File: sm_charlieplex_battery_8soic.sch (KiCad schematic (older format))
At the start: 14 parts, among them SW1 SW_Push, U1 ATtiny10-TS

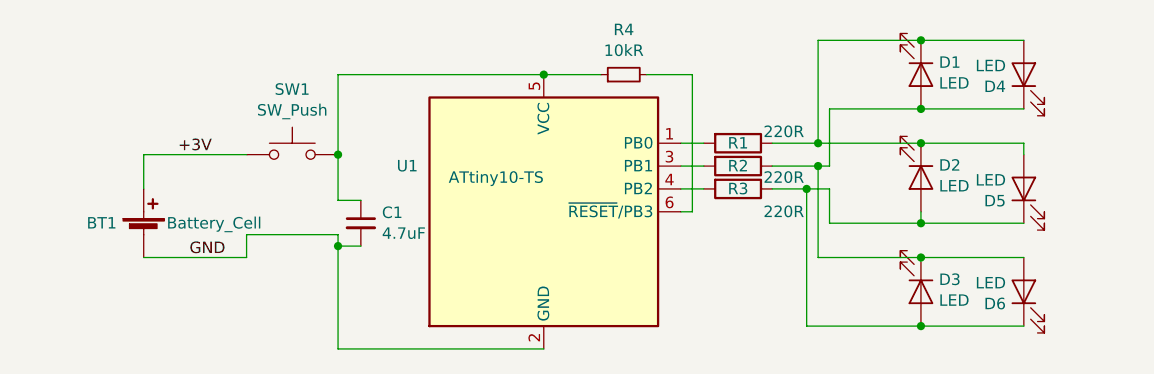
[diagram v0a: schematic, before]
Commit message: Reformat to use ATTiny402
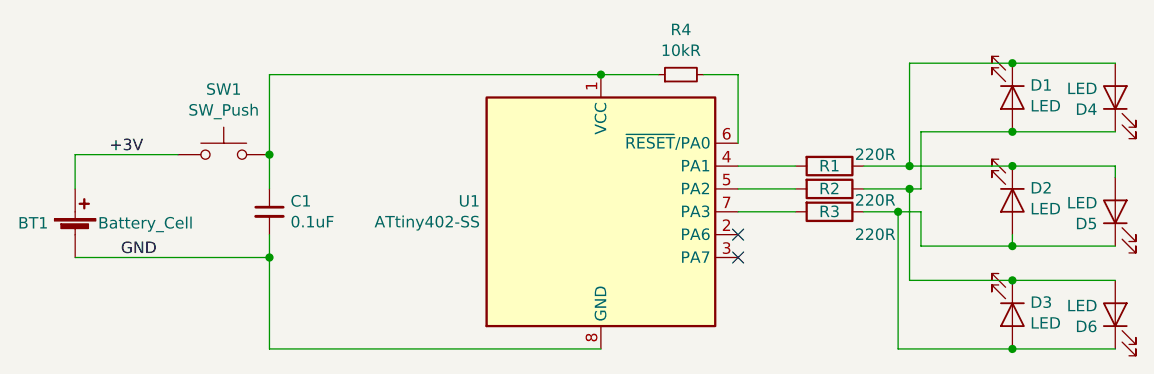
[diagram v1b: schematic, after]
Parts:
- removed U1: ATtiny10-TS, Package_TO_SOT_SMD:SOT-23-6, symbol MCU_Microchip_ATtiny:ATtiny10-TS
- added U1: ATtiny402-SS, Package_SO:SOIC-8_3.9x4.9mm_P1.27mm, symbol MCU_Microchip_ATtiny:ATtiny402-SS
- C1: value 4.7uF -> 0.1uF
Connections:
- net GND: now also U1.8 (GND)
- net at R1.2: now also U1.4 (PA1)
- net at R2.2: now also U1.5 (PA2)
- net at R3.2: now also U1.7 (PA3)
- net at C1.1, R4.1, SW1.2: now also U1.1 (VCC)
- net at R4.2: now also U1.6 (~RESET~/PA0)
- no-connect marks 0 -> 2
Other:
- moved on the sheet: BT1, C1, D1, D2, D3, D4, D5, D6, R1, R2, R3, R4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

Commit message: Some changes
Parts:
- removed U1: ATtiny402-SS, Package_SO:SOIC-8_3.9x4.9mm_P1.27mm, symbol MCU_Microchip_ATtiny:ATtiny402-SS
- added U1: ATtiny13A-SSU, Package_SO:SOIC-8_3.9x4.9mm_P1.27mm, symbol MCU_Microchip_ATtiny:ATtiny13A-SSU
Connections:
- net GND: now also U1.4 (GND)
- net at R1.2: now also U1.6 (PB1)
- net at R2.2: now also U1.7 (PB2)
- net at R3.2: now also U1.2 (PB3)
- net at C1.1, R4.1, SW1.2: now also U1.8 (VCC)
- net at R4.2: now also U1.1 (~RESET~/PB5)
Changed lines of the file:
@@
 Wire Wire Line
 	2850 3500 3300 3500
-$Comp
-L MCU_Microchip_ATtiny:ATtiny402-SS U1
-U 1 1 5DEC46B9
-P 5150 3750
-F 0 "U1" H 4621 3796 50  0000 R CNN
-F 1 "ATtiny402-SS" H 4621 3705 50  0000 R CNN
-F 2 "Package_SO:SOIC-8_3.9x4.9mm_P1.27mm" H 5150 3750 50  0001 C CIN
-F 3 "http://ww1.microchip.com/downloads/en/DeviceDoc/ATtiny202-402-AVR-MCU-with-Core-Independent-Peripherals_and-picoPower-40001969A.pdf" H 5150 3750 50  0001 C CNN
-	1    5150 3750
-	1    0    0    -1
-$EndComp
 Wire Wire Line
 	3700 3950 3700 3850
@@
 Connection ~ 3700 3950
 Wire Wire Line
-	5150 3150 5400 3150
-Connection ~ 5150 3150
-Wire Wire Line
-	5600 3150 5750 3150
-Wire Wire Line
-	5750 3150 5750 3450
-Wire Wire Line
 	5750 3550 6000 3550
 Wire Wire Line
@@
 	5750 3750 6000 3750
 NoConn ~ 5750 3850
-NoConn ~ 5750 3950
+Wire Wire Line
+	3700 4350 5150 4350
 Wire Wire Line
 	3700 3150 5150 3150
+$Comp
+L MCU_Microchip_ATtiny:ATtiny13A-SSU U1
+U 1 1 5DEBE77A
+P 5150 3750
+F 0 "U1" H 4620 3796 50  0000 R CNN
+F 1 "ATtiny13A-SSU" H 4620 3705 50  0000 R CNN
+F 2 "Package_SO:SOIC-8_3.9x4.9mm_P1.27mm" H 5150 3750 50  0001 C CIN
+F 3 "http://ww1.microchip.com/downloads/en/DeviceDoc/doc8126.pdf" H 5150 3750 50  0001 C CNN
+	1    5150 3750
+	1    0    0    -1
+$EndComp
+Connection ~ 5150 3150
 Wire Wire Line
-	3700 4350 5150 4350
+	5150 3150 5400 3150
+Wire Wire Line
+	5850 3150 5850 3950
+Wire Wire Line
+	5850 3950 5750 3950
+Wire Wire Line
+	5600 3150 5850 3150
+NoConn ~ 5750 3450
 $EndSCHEMATC
